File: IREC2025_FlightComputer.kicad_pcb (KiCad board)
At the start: 4 copper layers, 165.2 x 176 mm, 135 parts, among them J1 Molex Microfit, J2 BOOT0, J3 Companion, J4 Molex Microfit, J5 SWD, J6 Molex Microfit, J8 MEM2080-00-128-00-A_REVA, Q1 SI7232DN-T1-GE3, U1 STM32U575VGTx, U10 XL4015E1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

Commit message: ......
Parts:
- C14, C15, C27, C32, C34: moved to B.Cu
- C35: footprint 180uF:CAP_FKS_F_PAN -> Capacitor_SMD:CP_Elec_5x5.3
- C38: value 470uF -> 100uF; footprint Capacitor_SMD:CP_Elec_8x10 -> Capacitor_SMD:CP_Elec_5x5.3
- L3: value 68uH -> 33uH; footprint EasyEDA:IND-SMD_L22.5-W22.0 -> Inductor_SMD:L_Bourns_SRP1038C_10.0x10.0mm
- moved C27 269.3 mm to (162.9, 115.8)
- moved C34 268.7 mm to (162.9, 113.3)
- moved U5 180.9 mm to (228.1, 54.6)
- moved D4 141.0 mm to (224.4, 63.0)
- moved D5 141.0 mm to (232.2, 63.0)
- moved D8 134.6 mm to (-32.0, 76.1), turned to 90 degrees
- moved C21 131.1 mm to (228.1, 45.1)
- moved C74 131.1 mm to (231.9, 51.5)
- moved U7 103.1 mm to (-22.9, 84.6)
- moved L3 97.2 mm to (-31.7, 93.8), turned to -90 degrees
- moved C38 92.1 mm to (-6.62, 104.8)
- moved C35 80.1 mm to (-18.8, 118.4), turned to -90 degrees
- moved C37 69.7 mm to (-5.58, 116.4)
- moved R38 51.4 mm to (134.8, 104.2), turned to 135 degrees
- moved C22 51.1 mm to (133.8, 101.9), turned to 45 degrees
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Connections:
- D8 pad 1: +5V -> Net-(U7-OUT)
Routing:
- net eMMC_CMD: track 18.2 -> 61.0 mm, vias 2 -> 4
- net +3.3V: track 45.9 -> 59.5 mm, vias 14 -> 21
- net +3.3VA: track 0.03 -> 4.12 mm, vias 1 -> 2
- net nRST: track 0.00 -> 3.90 mm, vias 0 -> 1
- net +5V: track 1.68 -> 0.00 mm
- net Net-(U2-CAP): track 2.85 -> 1.42 mm, vias 2 -> 1
- net BAT_LEVEL: track 0.00 -> 1.23 mm, vias 0 -> 1
- net MMC_SDA: track 17.5 -> 16.9 mm, vias 2 -> 1
- net VBAT-: vias 3 -> 1
- removed copper zone on F.Cu, net +5V
- removed copper zone on F.Cu, net Net-(L1-Pad1)
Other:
- board text added: "RX"
- board text added: "TX"

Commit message: fkdjgfg
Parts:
- removed C35: 180uF, Capacitor_SMD:CP_Elec_5x5.3
- removed C37: 1uF, PCM_JLCPCB:C_0603
- removed C38: 100uF, Capacitor_SMD:CP_Elec_5x5.3
- removed D8: SS34_C466502, GNSS:DIOM7959X262N
- removed L3: 33uH, Inductor_SMD:L_Bourns_SRP1038C_10.0x10.0mm
- removed U7: XL1509-5.0, Package_SO:SOIC-8_3.9x4.9mm_P1.27mm
- L1: footprint EasyEDA:IND-SMD_L4.0-W4.0_XFL4020-102MEB -> newinductor:IND_EPCOS_B82432T_EPC
- moved C21 145.2 mm to (83.1, 53.0)
- moved C74 142.5 mm to (92.5, 81.2)
- moved U5 140.8 mm to (91.8, 89.8), turned to 90 degrees
- moved D5 139.6 mm to (94.5, 86.0)
- moved D4 138.3 mm to (88.0, 86.0)
- moved R18 128.4 mm to (38.8, 121.6), turned to 180 degrees
- moved LED1 126.4 mm to (38.8, 123.3), turned to 180 degrees
- moved R39 119.3 mm to (94.9, 72.3), turned to -90 degrees
- moved LED3 117.7 mm to (92.9, 72.4), turned to 90 degrees
- moved R2 70.1 mm to (77.6, 89.0)
- moved C17 66.4 mm to (79.7, 89.1), turned to 90 degrees
- moved D1 58.4 mm to (81.5, 91.8), turned to 180 degrees
- moved L1 24.7 mm to (84.3, 79.8)
- moved R10 24.4 mm to (78.0, 75.7)
- moved C20 24.3 mm to (74.9, 83.8)
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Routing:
- net PPS: track 0.00 -> 15.3 mm, vias 0 -> 2
- net BAT_LEVEL: track 1.23 -> 9.14 mm
- net eMMC_CLK: track 54.9 -> 61.4 mm, vias 3 -> 1
- net SERVO_B: track 48.2 -> 42.1 mm
- net Net-(LED3-Pad1): track 0.00 -> 2.01 mm
- net Net-(LED1-Pad2): track 0.00 -> 1.70 mm
- net +5V: track 0.00 -> 1.41 mm
- added copper zone on F.Cu, net +5V
- added copper zone on F.Cu, net Net-(D4-K)
- added copper zone on F.Cu, net Net-(L1-Pad1)

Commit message: Feat: Minor improvement
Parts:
- removed R28, R29, R30, R32, R33: 10kΩ, PCM_JLCPCB:R_0603
- removed R39: 1kΩ, PCM_JLCPCB:R_0603
- added C35: 180uF, Capacitor_SMD:CP_Elec_5x5.3, F.Cu at (47.5, 144.6)
- added C37: 1uF, PCM_JLCPCB:C_0603, F.Cu at (45.0, 155.9)
- added C38: 100uF, Capacitor_SMD:CP_Elec_5x5.3, F.Cu at (47.5, 151.4)
- added L3: 33uH, Inductor_SMD:L_Bourns_SRP1038C_10.0x10.0mm, F.Cu at (59.0, 147.1)
- added R36: 470Ω, PCM_JLCPCB:R_0603, F.Cu at (95.2, 72.4)
- added U7: XL1509-5.0, Package_SO:SOIC-8_3.9x4.9mm_P1.27mm, F.Cu at (56.2, 156.2)
- R18, R22: value 1kΩ -> 470Ω
- moved R22 275.5 mm to (151.6, 106.7), turned to 180 degrees
- moved PB0 268.4 mm to (151.6, 104.4), turned to 180 degrees
- moved RF1 2.59 mm to (156.7, 129.5)
- moved LED1 1.19 mm to (38.9, 124.5)
- moved H1 0.71 mm to (167.0, 130.5)
- moved R18 0.10 mm to (38.9, 121.7)
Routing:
- net VBAT-: track 0.65 -> 14.9 mm, vias 1 -> 9
- net GPIO_TEST: track 0.00 -> 12.6 mm, vias 0 -> 2
- net Net-(PB0-Pad1): track 0.00 -> 2.30 mm
- net Net-(U15-ANT): track 6.05 -> 7.44 mm
- net Net-(LED1-Pad2): track 1.70 -> 2.81 mm
- added copper zone on F.Cu, net (none)
- added copper zone on In2.Cu, net +3.3V
- removed copper zone on F.Cu, net Net-(D4-K)
- removed copper zone on F.Cu, net Net-(L1-Pad1)

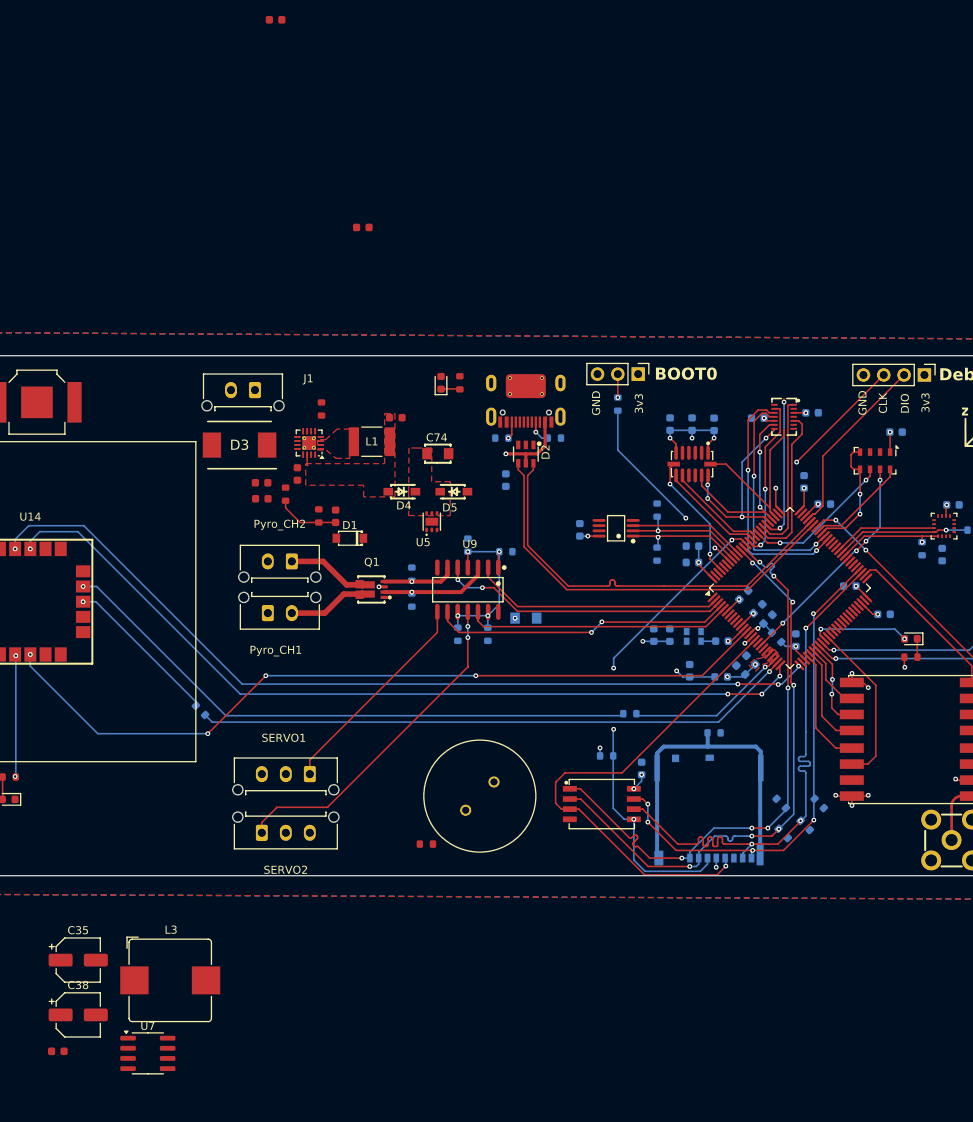
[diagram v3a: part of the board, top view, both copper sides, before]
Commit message: Feat: Finish superior LDO route
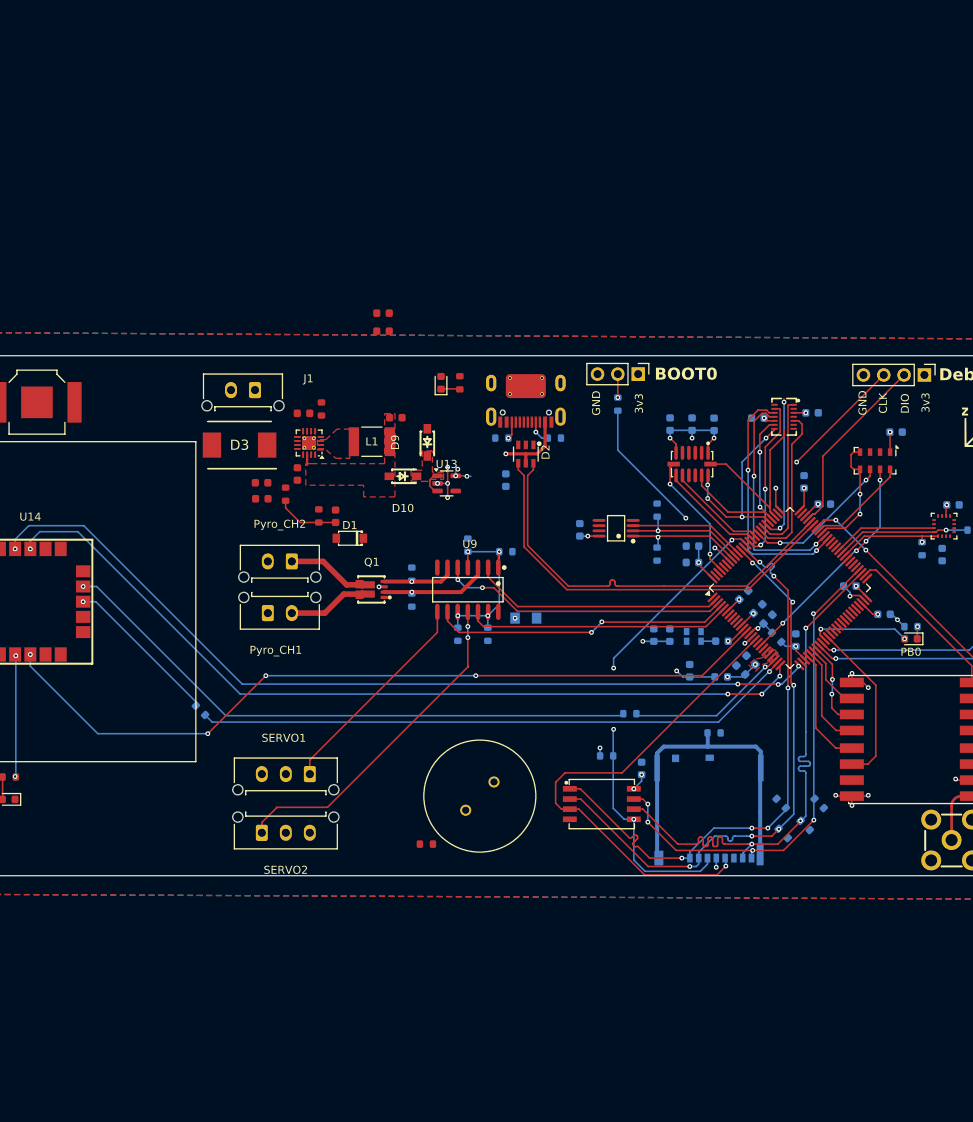
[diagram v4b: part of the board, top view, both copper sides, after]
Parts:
- removed C21: 2.2uF, PCM_JLCPCB:C_0603
- removed C35: 180uF, Capacitor_SMD:CP_Elec_5x5.3
- removed C37: 1uF, PCM_JLCPCB:C_0603
- removed C38: 100uF, Capacitor_SMD:CP_Elec_5x5.3
- removed C74: 100uF, EasyEDA:CAP-SMD_L3.2-W1.6
- removed D4, D5: NRVB120VLSFT1G, EasyEDA:SOD-123_L2.7-W1.6-LS3.7-RD-1
- removed L3: 33uH, Inductor_SMD:L_Bourns_SRP1038C_10.0x10.0mm
- removed U5: LP5912Q3.3DRVRQ1, EasyEDA:WSON-6_L2.0-W2.0-P0.65-TL-EP
- removed U7: XL1509-5.0, Package_SO:SOIC-8_3.9x4.9mm_P1.27mm
- added C39: 10uF, PCM_JLCPCB:C_0603, F.Cu at (85.6, 63.7)
- added C41: 10uF, PCM_JLCPCB:C_0603, F.Cu at (85.6, 65.9)
- added D10: NRVB120VLSFT1G, EasyEDA:SOD-123_L2.7-W1.6-LS3.7-RD-1, F.Cu at (88.1, 84.1)
- added D9: NRVB120VLSFT1G, EasyEDA:SOD-123_L2.7-W1.6-LS3.7-RD-1, F.Cu at (91.2, 79.8)
- added U13: TLV75733PDBV, Package_TO_SOT_SMD:SOT-23-5, F.Cu at (93.6, 85.0)
- R22: moved to B.Cu
- moved C25 49.3 mm to (75.7, 76.2)
- moved R22 3.81 mm to (151.6, 102.9)
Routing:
- net VBAT-: track 14.9 -> 24.8 mm, vias 9 -> 14
- net Net-(D10-K): track 0.00 -> 3.17 mm
- net +3.3V: track 59.5 -> 62.3 mm, vias 21 -> 24
- net Net-(PB0-Pad1): track 2.30 -> 1.54 mm, vias 0 -> 1
- added copper zone on F.Cu, net Net-(D10-K)

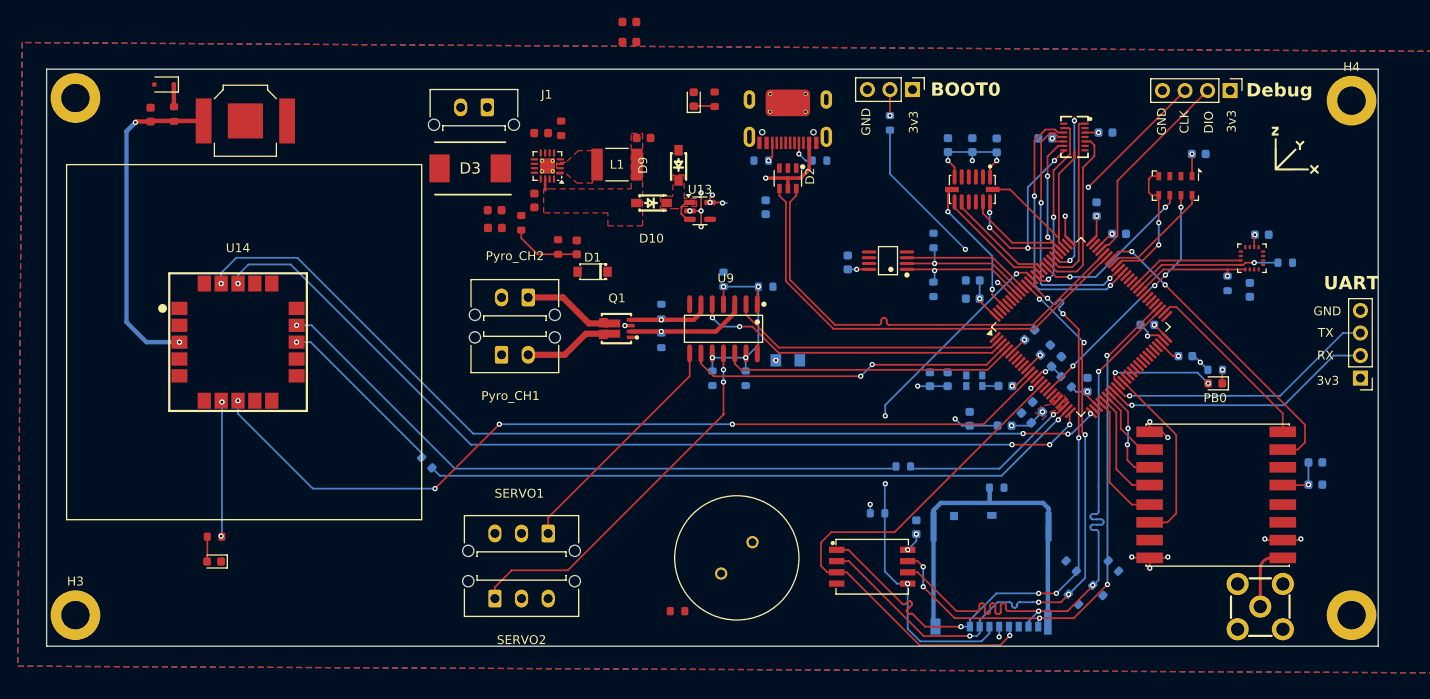
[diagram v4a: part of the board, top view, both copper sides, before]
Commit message: Feat: add silkscreen
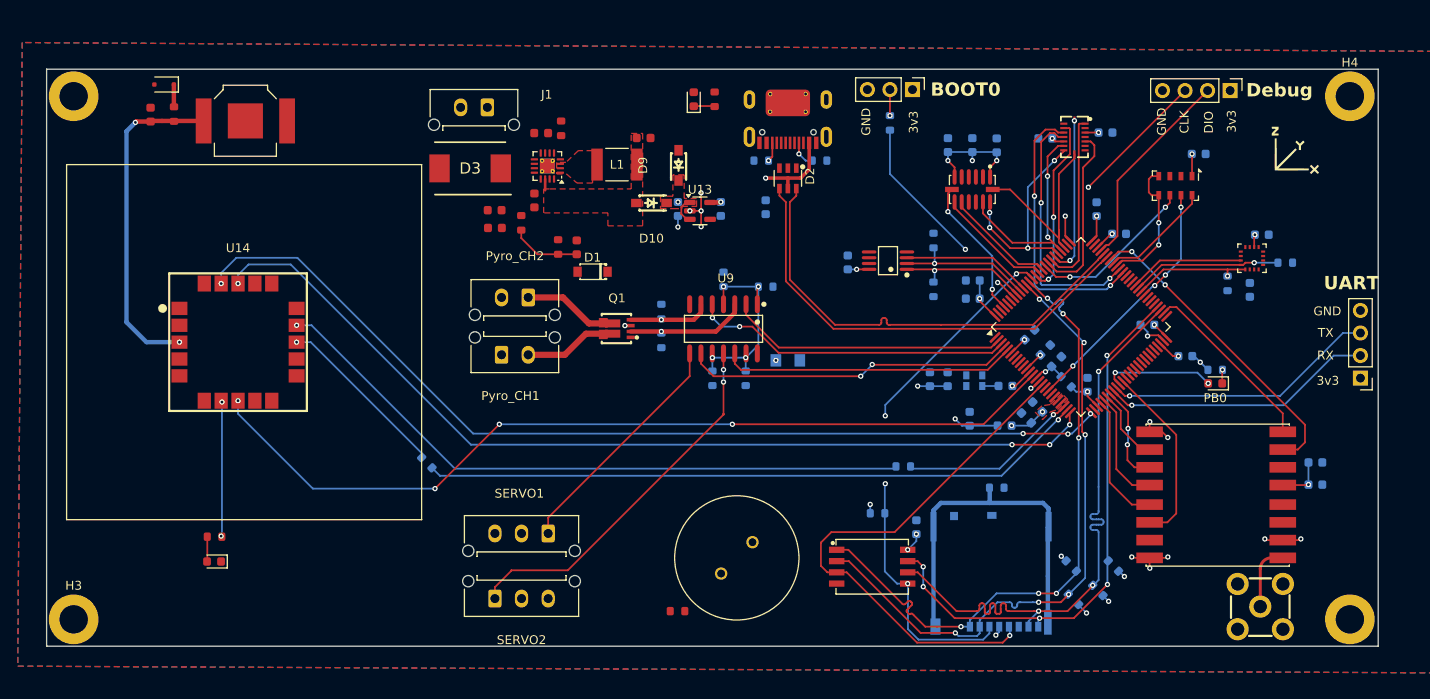
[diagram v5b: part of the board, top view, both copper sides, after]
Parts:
- added G***: LOGO, LOGO, B.Cu at (42.7, 121.5)
- C39, C41: moved to B.Cu
- moved C39 21.8 mm to (91.1, 84.7), turned to -90 degrees
- moved C41 21.4 mm to (95.9, 84.7), turned to -90 degrees
- moved H4 0.54 mm to (166.8, 72.0)
- moved H3 0.52 mm to (23.0, 131.0)
- moved H1 0.51 mm to (166.8, 131.0)
- moved H2 0.29 mm to (23.0, 72.0)
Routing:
- net +3.3V: track 62.3 -> 64.5 mm, vias 24 -> 26
- net VBAT-: track 24.8 -> 26.0 mm, vias 14 -> 15
- net Net-(D10-K): vias 0 -> 1
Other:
- board text added: "I need ibuprofen for real (Boonyakorn Tanrattanakorn was here)"
